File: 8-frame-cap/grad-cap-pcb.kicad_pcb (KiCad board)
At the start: 2 copper layers, 339.4 x 339.4 mm, 127 parts, among them J1 B02B-XASK-1LFSN, T1 PHPT610035PKX, T2 PHPT610035PKX, T3 PHPT610035PKX, T4 PHPT610035PKX, T5 PHPT610035PKX, T6 PHPT610035PKX, T7 PHPT610035PKX, U1 MC74HC73ADR2G, U2 SN74HCS238DYYR, U3 ICM7555xB, U4 SN74AHCT32DBR, U5 SN74AHCT32DBR

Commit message: routed traces, reorganized, renamed
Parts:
- removed the D50 at (334.5, 214.4)
- removed the D50 at (353.9, 236.1)
- added D18: 3, LED_SMD:LED_0805_2012Metric_Pad1.15x1.40mm_HandSolder, F.Cu at (213.0, 187.0)
- added D19: 1, LED_SMD:LED_0805_2012Metric_Pad1.15x1.40mm_HandSolder, F.Cu at (210.1, 229.4)
- added D50: 12, LED_SMD:LED_0805_2012Metric_Pad1.15x1.40mm_HandSolder, F.Cu at (321.2, 211.4)
- added D51: 2, LED_SMD:LED_0805_2012Metric_Pad1.15x1.40mm_HandSolder, F.Cu at (298.1, 207.4)
- added D52: 23, LED_SMD:LED_0805_2012Metric_Pad1.15x1.40mm_HandSolder, F.Cu at (285.7, 216.7)
- added D53: 3, LED_SMD:LED_0805_2012Metric_Pad1.15x1.40mm_HandSolder, F.Cu at (280.2, 228.5)
- added D54: 3, LED_SMD:LED_0805_2012Metric_Pad1.15x1.40mm_HandSolder, F.Cu at (325.6, 202.8)
- added D55: 1, LED_SMD:LED_0805_2012Metric_Pad1.15x1.40mm_HandSolder, F.Cu at (321.0, 188.1)
- added D56: 12, LED_SMD:LED_0805_2012Metric_Pad1.15x1.40mm_HandSolder, F.Cu at (312.9, 174.9)
- added D57: 2, LED_SMD:LED_0805_2012Metric_Pad1.15x1.40mm_HandSolder, F.Cu at (295.0, 166.0)
- added D58: 23, LED_SMD:LED_0805_2012Metric_Pad1.15x1.40mm_HandSolder, F.Cu at (340.6, 198.6)
- added D59: 3, LED_SMD:LED_0805_2012Metric_Pad1.15x1.40mm_HandSolder, F.Cu at (347.5, 186.7)
- added D60: 3, LED_SMD:LED_0805_2012Metric_Pad1.15x1.40mm_HandSolder, F.Cu at (358.3, 177.0)
- added D61: 1, LED_SMD:LED_0805_2012Metric_Pad1.15x1.40mm_HandSolder, F.Cu at (356.2, 215.0)
- added D62: 12, LED_SMD:LED_0805_2012Metric_Pad1.15x1.40mm_HandSolder, F.Cu at (375.9, 217.4)
- added D63: 2, LED_SMD:LED_0805_2012Metric_Pad1.15x1.40mm_HandSolder, F.Cu at (391.1, 224.6)
- added D64: 23, LED_SMD:LED_0805_2012Metric_Pad1.15x1.40mm_HandSolder, F.Cu at (341.6, 228.1)
- added D65: 3, LED_SMD:LED_0805_2012Metric_Pad1.15x1.40mm_HandSolder, F.Cu at (348.6, 242.1)
- added D66: 3, LED_SMD:LED_0805_2012Metric_Pad1.15x1.40mm_HandSolder, F.Cu at (350.0, 256.0)
- added D67: 1, LED_SMD:LED_0805_2012Metric_Pad1.15x1.40mm_HandSolder, F.Cu at (350.0, 270.0)
- added G***: LOGO, LOGO, F.Cu at (253.8, 102.2)
- added R31: R_Small_US, Resistor_SMD:R_0603_1608Metric_Pad0.98x0.95mm_HandSolder, F.Cu at (245.0, 153.0)
- added R63: R_Small_US, Resistor_SMD:R_0603_1608Metric_Pad0.98x0.95mm_HandSolder, F.Cu at (386.1, 222.4)
- added R64: R_Small_US, Resistor_SMD:R_0603_1608Metric_Pad0.98x0.95mm_HandSolder, F.Cu at (345.6, 234.1)
- added R65: R_Small_US, Resistor_SMD:R_0603_1608Metric_Pad0.98x0.95mm_HandSolder, F.Cu at (350.0, 248.0)
- added R66: R_Small_US, Resistor_SMD:R_0603_1608Metric_Pad0.98x0.95mm_HandSolder, F.Cu at (350.0, 261.0)
- added R67: R_Small_US, Resistor_SMD:R_0603_1608Metric_Pad0.98x0.95mm_HandSolder, F.Cu at (350.0, 276.0)
- added R68: R_Small_US, Resistor_SMD:R_0603_1608Metric_Pad0.98x0.95mm_HandSolder, F.Cu at (257.1, 375.2)
- added R69: R_Small_US, Resistor_SMD:R_0603_1608Metric_Pad0.98x0.95mm_HandSolder, F.Cu at (255.4, 377.0)
- added R70: 10K, Capacitor_SMD:C_0402_1005Metric_Pad0.74x0.62mm_HandSolder, F.Cu at (238.2, 370.0)
- added R71: 10K, Capacitor_SMD:C_0402_1005Metric_Pad0.74x0.62mm_HandSolder, F.Cu at (267.0, 362.3)
- added R72: 10k, Capacitor_SMD:C_0402_1005Metric_Pad0.74x0.62mm_HandSolder, B.Cu at (251.8, 354.6)
- added R73: 10k, Capacitor_SMD:C_0402_1005Metric_Pad0.74x0.62mm_HandSolder, B.Cu at (250.2, 354.6)
- added R74: 10k, Capacitor_SMD:C_0402_1005Metric_Pad0.74x0.62mm_HandSolder, B.Cu at (248.7, 354.6)
- added R75: 10k, Capacitor_SMD:C_0402_1005Metric_Pad0.74x0.62mm_HandSolder, F.Cu at (291.1, 364.0)
- added R76: 10k, Capacitor_SMD:C_0402_1005Metric_Pad0.74x0.62mm_HandSolder, F.Cu at (291.1, 366.0)
- added R77: 10k, Capacitor_SMD:C_0402_1005Metric_Pad0.74x0.62mm_HandSolder, F.Cu at (291.1, 368.0)
- added R78: 10k, Capacitor_SMD:C_0402_1005Metric_Pad0.74x0.62mm_HandSolder, F.Cu at (226.1, 351.0)
- added R79: 10k, Capacitor_SMD:C_0402_1005Metric_Pad0.74x0.62mm_HandSolder, F.Cu at (226.1, 353.0)
- added R80: 10k, Capacitor_SMD:C_0402_1005Metric_Pad0.74x0.62mm_HandSolder, F.Cu at (226.1, 355.0)
- added R81: 10K, Capacitor_SMD:C_0402_1005Metric_Pad0.74x0.62mm_HandSolder, F.Cu at (238.1, 365.0)
- added R82: 10K, Capacitor_SMD:C_0402_1005Metric_Pad0.74x0.62mm_HandSolder, F.Cu at (241.6, 358.3)
- added R83: 10K, Capacitor_SMD:C_0402_1005Metric_Pad0.74x0.62mm_HandSolder, F.Cu at (235.2, 370.0)
- added R84: 10K, Capacitor_SMD:C_0402_1005Metric_Pad0.74x0.62mm_HandSolder, F.Cu at (267.0, 364.8)
- added U6: MC74HC73ADR2G, GRAD-CAP:MC74HC73ADR2G_JK-FLIPFLOP, F.Cu at (259.0, 360.5)
- C1: value C_Small_US -> C_Small; footprint Capacitor_SMD:C_0805_2012Metric_Pad1.18x1.45mm_HandSolder -> Capacitor_SMD:C_0603_1608Metric_Pad1.08x0.95mm_HandSolder
- C2: value .1uF -> C_Small_US; footprint Capacitor_SMD:C_0805_2012Metric_Pad1.18x1.45mm_HandSolder -> Capacitor_SMD:C_0603_1608Metric_Pad1.08x0.95mm_HandSolder
- C3: value C_Small -> .1uF; footprint Capacitor_SMD:C_0805_2012Metric_Pad1.18x1.45mm_HandSolder -> Capacitor_SMD:C_0603_1608Metric_Pad1.08x0.95mm_HandSolder; moved to B.Cu
- D1, D28, D36, D8: footprint LED_SMD:LED_0603_1608Metric -> LED_SMD:LED_0805_2012Metric_Pad1.15x1.40mm_HandSolder
- D10: value 12 -> 23; footprint LED_SMD:LED_0603_1608Metric -> LED_SMD:LED_0805_2012Metric_Pad1.15x1.40mm_HandSolder
- D11, D30: value 6 -> 3; footprint LED_SMD:LED_0603_1608Metric -> LED_SMD:LED_0805_2012Metric_Pad1.15x1.40mm_HandSolder
- D12, D23, D24: value 67 -> 3; footprint LED_SMD:LED_0603_1608Metric -> LED_SMD:LED_0805_2012Metric_Pad1.15x1.40mm_HandSolder
- D13: value 56 -> 1; footprint LED_SMD:LED_0603_1608Metric -> LED_SMD:LED_0805_2012Metric_Pad1.15x1.40mm_HandSolder
- D14: value 6 -> 12; footprint LED_SMD:LED_0603_1608Metric -> LED_SMD:LED_0805_2012Metric_Pad1.15x1.40mm_HandSolder
- D15: value 6 -> 2; footprint LED_SMD:LED_0603_1608Metric -> LED_SMD:LED_0805_2012Metric_Pad1.15x1.40mm_HandSolder
- D16: value 1 -> 23; footprint LED_SMD:LED_0603_1608Metric -> LED_SMD:LED_0805_2012Metric_Pad1.15x1.40mm_HandSolder
- D17, D42: value 23 -> 3; footprint LED_SMD:LED_0603_1608Metric -> LED_SMD:LED_0805_2012Metric_Pad1.15x1.40mm_HandSolder
- D2, D32: value 4 -> 12; footprint LED_SMD:LED_0603_1608Metric -> LED_SMD:LED_0805_2012Metric_Pad1.15x1.40mm_HandSolder
- D20: value 2 -> 12; footprint LED_SMD:LED_0603_1608Metric -> LED_SMD:LED_0805_2012Metric_Pad1.15x1.40mm_HandSolder
- D21: value 67 -> 2; footprint LED_SMD:LED_0603_1608Metric -> LED_SMD:LED_0805_2012Metric_Pad1.15x1.40mm_HandSolder
- D22: value 7 -> 23; footprint LED_SMD:LED_0603_1608Metric -> LED_SMD:LED_0805_2012Metric_Pad1.15x1.40mm_HandSolder
- D25: value 6 -> 1; footprint LED_SMD:LED_0603_1608Metric -> LED_SMD:LED_0805_2012Metric_Pad1.15x1.40mm_HandSolder
- D26: value 32 -> 12; footprint LED_SMD:LED_0603_1608Metric -> LED_SMD:LED_0805_2012Metric_Pad1.15x1.40mm_HandSolder
- D27: value 1 -> 2; footprint LED_SMD:LED_0603_1608Metric -> LED_SMD:LED_0805_2012Metric_Pad1.15x1.40mm_HandSolder
- D29: value 7 -> 3; footprint LED_SMD:LED_0603_1608Metric -> LED_SMD:LED_0805_2012Metric_Pad1.15x1.40mm_HandSolder
- D3: value 56 -> 2; footprint LED_SMD:LED_0603_1608Metric -> LED_SMD:LED_0805_2012Metric_Pad1.15x1.40mm_HandSolder
- D31: value 7 -> 1; footprint LED_SMD:LED_0603_1608Metric -> LED_SMD:LED_0805_2012Metric_Pad1.15x1.40mm_HandSolder
- D33, D45: value 7 -> 2; footprint LED_SMD:LED_0603_1608Metric -> LED_SMD:LED_0805_2012Metric_Pad1.15x1.40mm_HandSolder
- D34: value 3 -> 23; footprint LED_SMD:LED_0603_1608Metric -> LED_SMD:LED_0805_2012Metric_Pad1.15x1.40mm_HandSolder
- D35: value 12 -> 3; footprint LED_SMD:LED_0603_1608Metric -> LED_SMD:LED_0805_2012Metric_Pad1.15x1.40mm_HandSolder
- D37: value 8 -> 1; footprint LED_SMD:LED_0603_1608Metric -> LED_SMD:LED_0805_2012Metric_Pad1.15x1.40mm_HandSolder
- D38: value 67 -> 12; footprint LED_SMD:LED_0603_1608Metric -> LED_SMD:LED_0805_2012Metric_Pad1.15x1.40mm_HandSolder
- D39: value 45 -> 2; footprint LED_SMD:LED_0603_1608Metric -> LED_SMD:LED_0805_2012Metric_Pad1.15x1.40mm_HandSolder
- D4, D46: value 5 -> 23; footprint LED_SMD:LED_0603_1608Metric -> LED_SMD:LED_0805_2012Metric_Pad1.15x1.40mm_HandSolder
- D40: value 8 -> 23; footprint LED_SMD:LED_0603_1608Metric -> LED_SMD:LED_0805_2012Metric_Pad1.15x1.40mm_HandSolder
- D41: value 8 -> 3; footprint LED_SMD:LED_0603_1608Metric -> LED_SMD:LED_0805_2012Metric_Pad1.15x1.40mm_HandSolder
- D43: value 3 -> 1; footprint LED_SMD:LED_0603_1608Metric -> LED_SMD:LED_0805_2012Metric_Pad1.15x1.40mm_HandSolder
- D44: value 5 -> 12; footprint LED_SMD:LED_0603_1608Metric -> LED_SMD:LED_0805_2012Metric_Pad1.15x1.40mm_HandSolder
- D47: value 5 -> 3; footprint LED_SMD:LED_0603_1608Metric -> LED_SMD:LED_0805_2012Metric_Pad1.15x1.40mm_HandSolder
- D48: value 81 -> 3; footprint LED_SMD:LED_0603_1608Metric -> LED_SMD:LED_0805_2012Metric_Pad1.15x1.40mm_HandSolder
- D49: value 81 -> 1; footprint LED_SMD:LED_0603_1608Metric -> LED_SMD:LED_0805_2012Metric_Pad1.15x1.40mm_HandSolder
- D5, D6: value 56 -> 3; footprint LED_SMD:LED_0603_1608Metric -> LED_SMD:LED_0805_2012Metric_Pad1.15x1.40mm_HandSolder
- D7: value 12 -> 1; footprint LED_SMD:LED_0603_1608Metric -> LED_SMD:LED_0805_2012Metric_Pad1.15x1.40mm_HandSolder
- D9: value 12 -> 2; footprint LED_SMD:LED_0603_1608Metric -> LED_SMD:LED_0805_2012Metric_Pad1.15x1.40mm_HandSolder
- R1, R3: value 10K -> R_Small_US; footprint Resistor_SMD:R_0805_2012Metric_Pad1.20x1.40mm_HandSolder -> Resistor_SMD:R_0603_1608Metric_Pad0.98x0.95mm_HandSolder
- R10, R11, R12, R13, R5, R6, R7, R8, R9: value 10k -> R_Small_US; footprint Capacitor_SMD:C_0805_2012Metric_Pad1.18x1.45mm_HandSolder -> Resistor_SMD:R_0603_1608Metric_Pad0.98x0.95mm_HandSolder
- R14, R15, R16, R17, R18, R19, R2, R20, R21, R22, R23, R24, R25, R26, R27, R28, R29, R30, R32, R33, R34, R35, R36, R37, R38, R39, R4, R40, R41, R42, R43, R44, R45, R46, R47, R48, R49, R50, R51, R52, R53, R54, R55, R56, R57, R58, R59, R60, R61, R62: footprint Resistor_SMD:R_0805_2012Metric_Pad1.20x1.40mm_HandSolder -> Resistor_SMD:R_0603_1608Metric_Pad0.98x0.95mm_HandSolder
- U1: value MC74HC73ADR2G -> ICM7555xB; footprint GRAD-CAP:MC74HC73ADR2G_JK-FLIPFLOP -> Package_SO:SOIC-8_3.9x4.9mm_P1.27mm
- U2: value SN74HCS238DYYR -> MC74HC73ADR2G; footprint GRAD-CAP:SN74HCS238DYYR-3-8-MUX -> GRAD-CAP:MC74HC73ADR2G_JK-FLIPFLOP
- U3: value ICM7555xB -> SN74HCS238DYYR; footprint Package_SO:SOIC-8_3.9x4.9mm_P1.27mm -> GRAD-CAP:SN74HCS238DYYR-3-8-MUX
- moved R30 188.5 mm to (175.7, 156.3), turned to 45 degrees
- moved D8 175.0 mm to (186.0, 263.0), turned to -112.5 degrees
- moved D9 171.5 mm to (185.0, 280.2), turned to -90 degrees
- moved D45 166.0 mm to (279.6, 293.8), turned to -112.5 degrees
- moved R12 163.1 mm to (139.0, 241.0), turned to -157.5 degrees
- moved D32 162.8 mm to (230.7, 131.7), turned to -45 degrees
- moved R49 156.2 mm to (333.0, 220.0), turned to 22.5 degrees
- moved R11 154.6 mm to (158.0, 234.0), turned to -157.5 degrees
- moved D17 151.7 mm to (208.0, 196.0), turned to -112.5 degrees
- moved R34 149.5 mm to (261.3, 140.7), turned to 45 degrees
- moved R50 146.3 mm to (316.0, 209.0), turned to -22.5 degrees
- moved R57 144.1 mm to (288.0, 165.0), turned to 0 degrees
- moved D33 142.6 mm to (213.0, 120.0), turned to -22.5 degrees
- moved D36 142.5 mm to (294.0, 117.0), turned to 180 degrees
- moved R13 139.8 mm to (185.0, 220.0), turned to 112.5 degrees
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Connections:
- C1 pad 1: /555-pin2-6 -> /555-pin5
- C2 pad 1: +3.3V -> /555-pin2-6
- C3 pad 1: /555-pin5 -> +3.3V
- R1 pad 1: +3.3V -> /leds+mosfets/6c
- R1 pad 2: /u4-pu-r2 -> Net-(D1-A)
- R10 pad 1: /leds+mosfets/u3-pd-3y -> /leds+mosfets/6or7
- R10 pad 2: GND -> Net-(D10-A)
- R11 pad 1: /leds+mosfets/u8-pd2y -> /leds+mosfets/6c
- R11 pad 2: GND -> Net-(D11-A)
- R12 pad 1: /leds+mosfets/u8-pd2b -> /leds+mosfets/1c
- R12 pad 2: GND -> Net-(D12-A)
- R13 pad 1: /leds+mosfets/u8-pd2a -> /leds+mosfets/6or7
- R13 pad 2: GND -> Net-(D13-A)
- R14 pad 1: /leds+mosfets/frame1 -> /leds+mosfets/6c
- R14 pad 2: Net-(D1-A) -> Net-(D14-A)
- R15 pad 1: /leds+mosfets/frame4 -> /leds+mosfets/1c
- R15 pad 2: Net-(D2-A) -> Net-(D15-A)
- R16 pad 1: /leds+mosfets/5or6 -> /leds+mosfets/6or7
- R16 pad 2: Net-(D3-A) -> Net-(D16-A)
- R17 pad 1: Net-(D4-A) -> /leds+mosfets/6c
- R17 pad 2: /leds+mosfets/frame5 -> Net-(D17-A)
- R18 pad 1: /leds+mosfets/5or6 -> /leds+mosfets/1c
- R18 pad 2: Net-(D5-A) -> Net-(D18-A)
- R19 pad 1: /leds+mosfets/5or6 -> /leds+mosfets/6or7
- R19 pad 2: Net-(D6-A) -> Net-(D19-A)
- R2 pad 1: 555-power -> /leds+mosfets/1c
- R2 pad 2: /555-pin7 -> Net-(D2-A)
- R20 pad 1: /leds+mosfets/1or2 -> /leds+mosfets/6c
- R20 pad 2: Net-(D7-A) -> Net-(D20-A)
- R21 pad 1: /leds+mosfets/1or2 -> /leds+mosfets/4c
- R21 pad 2: Net-(D8-A) -> Net-(D21-A)
- R22 pad 1: /leds+mosfets/1or2 -> /leds+mosfets/10c
- R22 pad 2: Net-(D9-A) -> Net-(D22-A)
- R23 pad 1: /leds+mosfets/1or2 -> /leds+mosfets/2or3
- R23 pad 2: Net-(D10-A) -> Net-(D23-A)
- R24 pad 1: /leds+mosfets/frame6 -> /leds+mosfets/6c
- R24 pad 2: Net-(D11-A) -> Net-(D24-A)
- R25 pad 1: /leds+mosfets/6or7 -> /leds+mosfets/2c
- R25 pad 2: Net-(D12-A) -> Net-(D25-A)
- R26 pad 1: Net-(D13-A) -> /leds+mosfets/2or3
- R26 pad 2: /leds+mosfets/5or6 -> Net-(D26-A)
- R27 pad 1: /leds+mosfets/frame6 -> /leds+mosfets/3c
- R27 pad 2: Net-(D14-A) -> Net-(D27-A)
- R28 pad 1: /leds+mosfets/frame6 -> /leds+mosfets/2or3
- R28 pad 2: Net-(D15-A) -> Net-(D28-A)
- R29 pad 1: /leds+mosfets/frame1 -> /leds+mosfets/3c
- R29 pad 2: Net-(D16-A) -> Net-(D29-A)
- R3 pad 1: +3.3V -> /leds+mosfets/1or2
- R3 pad 2: /ff-reset -> Net-(D3-A)
- R30 pad 1: /leds+mosfets/2or3 -> /leds+mosfets/4c
- R30 pad 2: Net-(D17-A) -> Net-(D30-A)
- R32 pad 1: /leds+mosfets/frame2 -> /leds+mosfets/2or3
- R32 pad 2: Net-(D20-A) -> Net-(D32-A)
- R33 pad 1: /leds+mosfets/6or7 -> /leds+mosfets/3c
- R33 pad 2: Net-(D21-A) -> Net-(D33-A)
- R34 pad 1: /leds+mosfets/frame7 -> /leds+mosfets/11c
- R34 pad 2: Net-(D22-A) -> Net-(D34-A)
- R35 pad 1: Net-(D23-A) -> /leds+mosfets/11c
- R35 pad 2: /leds+mosfets/6or7 -> Net-(D35-A)
- R36 pad 1: /leds+mosfets/6or7 -> /leds+mosfets/13c
- R36 pad 2: Net-(D24-A) -> Net-(D36-A)
- R37 pad 1: /leds+mosfets/frame6 -> /leds+mosfets/2c
- R37 pad 2: Net-(D25-A) -> Net-(D37-A)
- R38 pad 2: Net-(D26-A) -> Net-(D38-A)
- R39 pad 1: /leds+mosfets/frame1 -> /leds+mosfets/3c
- R39 pad 2: Net-(D27-A) -> Net-(D39-A)
- R4 pad 1: /555-pin7 -> /leds+mosfets/2or3
- R4 pad 2: /555-pin2-6 -> Net-(D4-A)
- R40 pad 1: /leds+mosfets/2or3 -> /leds+mosfets/4c
- R40 pad 2: Net-(D28-A) -> Net-(D40-A)
- R41 pad 1: /leds+mosfets/frame7 -> /leds+mosfets/1or2
- R41 pad 2: Net-(D29-A) -> Net-(D41-A)
- R42 pad 1: /leds+mosfets/frame6 -> /leds+mosfets/2or3
- R42 pad 2: Net-(D30-A) -> Net-(D42-A)
- R43 pad 1: Net-(D31-A) -> /leds+mosfets/3c
- R43 pad 2: /leds+mosfets/frame7 -> Net-(D43-A)
- R44 pad 1: /leds+mosfets/frame4 -> /leds+mosfets/6or7
- R44 pad 2: Net-(D32-A) -> Net-(D44-A)
- R45 pad 1: /leds+mosfets/frame7 -> /leds+mosfets/6c
- R45 pad 2: Net-(D33-A) -> Net-(D45-A)
- R46 pad 1: /leds+mosfets/frame3 -> /leds+mosfets/1c
- R46 pad 2: Net-(D34-A) -> Net-(D46-A)
- R47 pad 2: Net-(D35-A) -> Net-(D47-A)
- R48 pad 1: /leds+mosfets/frame3 -> /leds+mosfets/9c
- R48 pad 2: Net-(D36-A) -> Net-(D48-A)
- R49 pad 1: /leds+mosfets/frame8 -> /leds+mosfets/11c
- R49 pad 2: Net-(D37-A) -> Net-(D49-A)
- R5 pad 1: /pd-mux-g0 -> /leds+mosfets/3c
- R5 pad 2: GND -> Net-(D5-A)
- R50 pad 1: /leds+mosfets/6or7 -> /leds+mosfets/13c
- R50 pad 2: Net-(D38-A) -> Net-(D50-A)
- R51 pad 1: /leds+mosfets/4or5 -> /leds+mosfets/4c
- R51 pad 2: Net-(D39-A) -> Net-(D51-A)
- R52 pad 1: /leds+mosfets/frame8 -> /leds+mosfets/10c
- R52 pad 2: Net-(D40-A) -> Net-(D52-A)
- R53 pad 1: /leds+mosfets/frame8 -> /leds+mosfets/6or7
- R53 pad 2: Net-(D41-A) -> Net-(D53-A)
- R54 pad 1: /leds+mosfets/2or3 -> /leds+mosfets/13c
- R54 pad 2: Net-(D42-A) -> Net-(D54-A)
- R55 pad 1: /leds+mosfets/frame3 -> /leds+mosfets/4c
- R55 pad 2: Net-(D43-A) -> Net-(D55-A)
- R56 pad 1: /leds+mosfets/frame5 -> /leds+mosfets/10c
- R56 pad 2: Net-(D44-A) -> Net-(D56-A)
- R57 pad 1: /leds+mosfets/frame7 -> /leds+mosfets/6or7
- R57 pad 2: Net-(D45-A) -> Net-(D57-A)
- R58 pad 1: Net-(D46-A) -> /leds+mosfets/12c
- R58 pad 2: /leds+mosfets/frame5 -> Net-(D58-A)
- R59 pad 1: /leds+mosfets/frame5 -> /leds+mosfets/10c
- R59 pad 2: Net-(D47-A) -> Net-(D59-A)
- R6 pad 1: /pd-mux-g1 -> /leds+mosfets/4c
- R6 pad 2: GND -> Net-(D6-A)
- R60 pad 1: /leds+mosfets/8or1 -> /leds+mosfets/14c
- R60 pad 2: Net-(D48-A) -> Net-(D60-A)
- R61 pad 1: /leds+mosfets/8or1 -> /leds+mosfets/4c
- R61 pad 2: Net-(D49-A) -> Net-(D61-A)
- R62 pad 1: /leds+mosfets/8or1 -> /leds+mosfets/10c
- R7 pad 1: /pd-mux-g2 -> /leds+mosfets/6or7
- R7 pad 2: GND -> Net-(D7-A)
- R8 pad 1: /leds+mosfets/u3-pd-3b -> /leds+mosfets/6c
- R8 pad 2: GND -> Net-(D8-A)
- R9 pad 1: /leds+mosfets/u3-pd-3a -> /leds+mosfets/1c
- R9 pad 2: GND -> Net-(D9-A)
- T1 pad 2: f6or7 -> f1or8
- T1 pad 4: 2 -> 1
- T1 pad 5: /leds+mosfets/frame3 -> /leds+mosfets/2c
- T1 pad 6: /leds+mosfets/frame3 -> /leds+mosfets/2c
- T1 pad 7: /leds+mosfets/6or7 -> /leds+mosfets/1c
- T1 pad 8: /leds+mosfets/6or7 -> /leds+mosfets/1c
- T2 pad 2: 1 -> f3or4
- T2 pad 4: 6 -> f4or5
- T2 pad 5: /leds+mosfets/frame7 -> /leds+mosfets/4c
- T2 pad 6: /leds+mosfets/frame7 -> /leds+mosfets/4c
- T2 pad 7: /leds+mosfets/frame2 -> /leds+mosfets/3c
- T2 pad 8: /leds+mosfets/frame2 -> /leds+mosfets/3c
- T3 pad 2: 5 -> f2or3
- T3 pad 4: unconnected-(T3-BASE-Pad4) -> f7or8
- T3 pad 5: /leds+mosfets/frame5 -> /leds+mosfets/6c
- T3 pad 6: /leds+mosfets/frame5 -> /leds+mosfets/6c
- T3 pad 7: /leds+mosfets/frame6 -> /leds+mosfets/2or3
- T3 pad 8: /leds+mosfets/frame6 -> /leds+mosfets/2or3
- T4 pad 2: 3 -> f1or2
- T4 pad 4: f4or5 -> f6or7
- T4 pad 5: /leds+mosfets/4or5 -> /leds+mosfets/6or7
- T4 pad 6: /leds+mosfets/4or5 -> /leds+mosfets/6or7
- T4 pad 7: /leds+mosfets/frame4 -> /leds+mosfets/1or2
- T4 pad 8: /leds+mosfets/frame4 -> /leds+mosfets/1or2
- T5 pad 2: f5or6 -> 2
- T5 pad 4: 0 -> f5or6
- T5 pad 5: /leds+mosfets/frame1 -> /leds+mosfets/10c
- T5 pad 6: /leds+mosfets/frame1 -> /leds+mosfets/10c
- T5 pad 7: /leds+mosfets/5or6 -> /leds+mosfets/9c
- T5 pad 8: /leds+mosfets/5or6 -> /leds+mosfets/9c
- T6 pad 2: 7 -> 3
- T6 pad 4: f1or8 -> 5
- T6 pad 5: /leds+mosfets/8or1 -> /leds+mosfets/12c
- T6 pad 6: /leds+mosfets/8or1 -> /leds+mosfets/12c
- T6 pad 7: /leds+mosfets/frame8 -> /leds+mosfets/11c
- T6 pad 8: /leds+mosfets/frame8 -> /leds+mosfets/11c
- T7 pad 2: f1or2 -> 4
- T7 pad 4: f2or3 -> 6
- T7 pad 5: /leds+mosfets/2or3 -> /leds+mosfets/14c
- T7 pad 6: /leds+mosfets/2or3 -> /leds+mosfets/14c
- T7 pad 7: /leds+mosfets/1or2 -> /leds+mosfets/13c
- T7 pad 8: /leds+mosfets/1or2 -> /leds+mosfets/13c
- U1 pad 1: CLOCK1 -> GND
- U1 pad 2: /ff-reset -> /555-pin2-6
- U1 pad 3: /ff-reset -> 555-PULSE
- U1 pad 4: +3.3V -> Net-(U1-R)
- U1 pad 5: CLOCK2 -> /555-pin5
- U1 pad 6: /ff-reset -> /555-pin2-6
- U1 pad 7: /ff-reset -> /555-pin7
- U1 pad 8: unconnected-(U1-*Q2-Pad8) -> Net-(U1-R)
- U2 pad 1: CLOCK1 -> 555-PULSE
- U2 pad 10: 5 -> /u4-pu-r2
- U2 pad 11: 4 -> GND
- U2 pad 12: 3 -> CLOCK1
- U2 pad 13: 2 -> Net-(U2-*Q1)
- U2 pad 14: 1 -> /u4-pu-r2
- U2 pad 2: CLOCK2 -> /ff-reset
- U2 pad 3: CLOCK3 -> /ff-reset
- U2 pad 4: /pd-mux-g0 -> +3.3V
- U2 pad 5: /pd-mux-g1 -> CLOCK1
- U2 pad 6: /pd-mux-g2 -> /ff-reset
- U2 pad 7: 7 -> /ff-reset
- U2 pad 8: GND -> Net-(U2-*Q1)
- U2 pad 9: 6 -> CLOCK2
- U3 pad 1: GND -> CLOCK1
- U3 pad 2: /555-pin2-6 -> CLOCK2
- U3 pad 3: CLOCK1 -> CLOCK3
- U3 pad 4: 555-power -> /pd-mux-g0
- U3 pad 5: /555-pin5 -> /pd-mux-g1
- U3 pad 6: /555-pin2-6 -> /pd-mux-g2
- U3 pad 7: /555-pin7 -> 7
- U3 pad 8: 555-power -> GND
- U5 pad 10: /leds+mosfets/u8-pd2a -> 7
- U5 pad 8: /leds+mosfets/u8-pd2y -> f7or8
- U5 pad 9: /leds+mosfets/u8-pd2b -> 6
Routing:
- net /leds+mosfets/6or7: track 0.00 -> 593.1 mm, vias 0 -> 8
- net /leds+mosfets/4c: track 0.00 -> 498.6 mm, vias 0 -> 11
- net /leds+mosfets/3c: track 0.00 -> 458.8 mm, vias 0 -> 6
- net /leds+mosfets/10c: track 0.00 -> 458.6 mm, vias 0 -> 6
- net /leds+mosfets/2or3: track 0.00 -> 407.3 mm, vias 0 -> 2
- net /leds+mosfets/1c: track 0.00 -> 369.1 mm, vias 0 -> 6
- net /leds+mosfets/6c: track 0.00 -> 360.8 mm, vias 0 -> 4
- net /leds+mosfets/13c: track 0.00 -> 299.2 mm, vias 0 -> 6
- net /leds+mosfets/11c: track 0.00 -> 290.5 mm, vias 0 -> 6
- net /leds+mosfets/1or2: track 0.00 -> 257.5 mm, vias 1 -> 10
- net /leds+mosfets/2c: track 0.00 -> 215.6 mm, vias 0 -> 4
- net /leds+mosfets/14c: track 0.00 -> 197.4 mm, vias 0 -> 4
- net /leds+mosfets/12c: track 0.00 -> 167.8 mm, vias 0 -> 4
- net /leds+mosfets/9c: track 0.00 -> 140.0 mm, vias 0 -> 2
- net CLOCK1: track 37.4 -> 9.35 mm, vias 2 -> 0
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- removed copper zone on F.Cu, net +3.3V
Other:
- board text removed: "1"
- board text removed: "2"
- board text removed: "24 cm"
- board text removed: "3"
- board text removed: "4"
- board text removed: "5"
- board text removed: "6"
- board text removed: "7"
- board text removed: "8"
- board text removed: "chud - billions must graduate chicken on raft"
- board text removed: "little bigger than 2 cm"
- board text removed: "w"

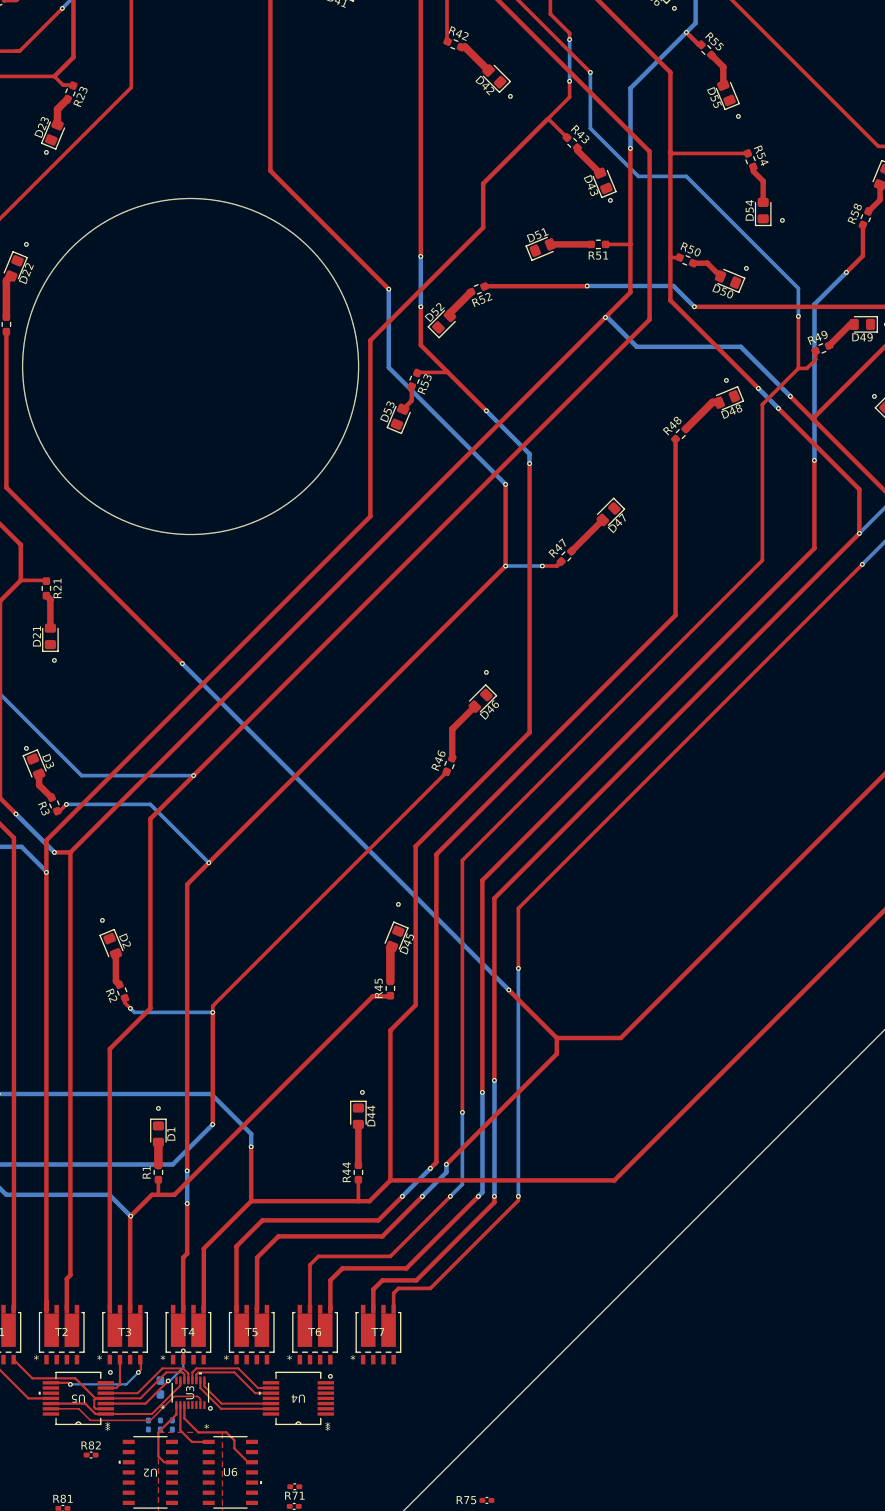
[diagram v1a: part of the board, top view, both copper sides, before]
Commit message: reorganized
horizontal -> vertical pin headers
traces added
moved components
switched clocks crystal-> si
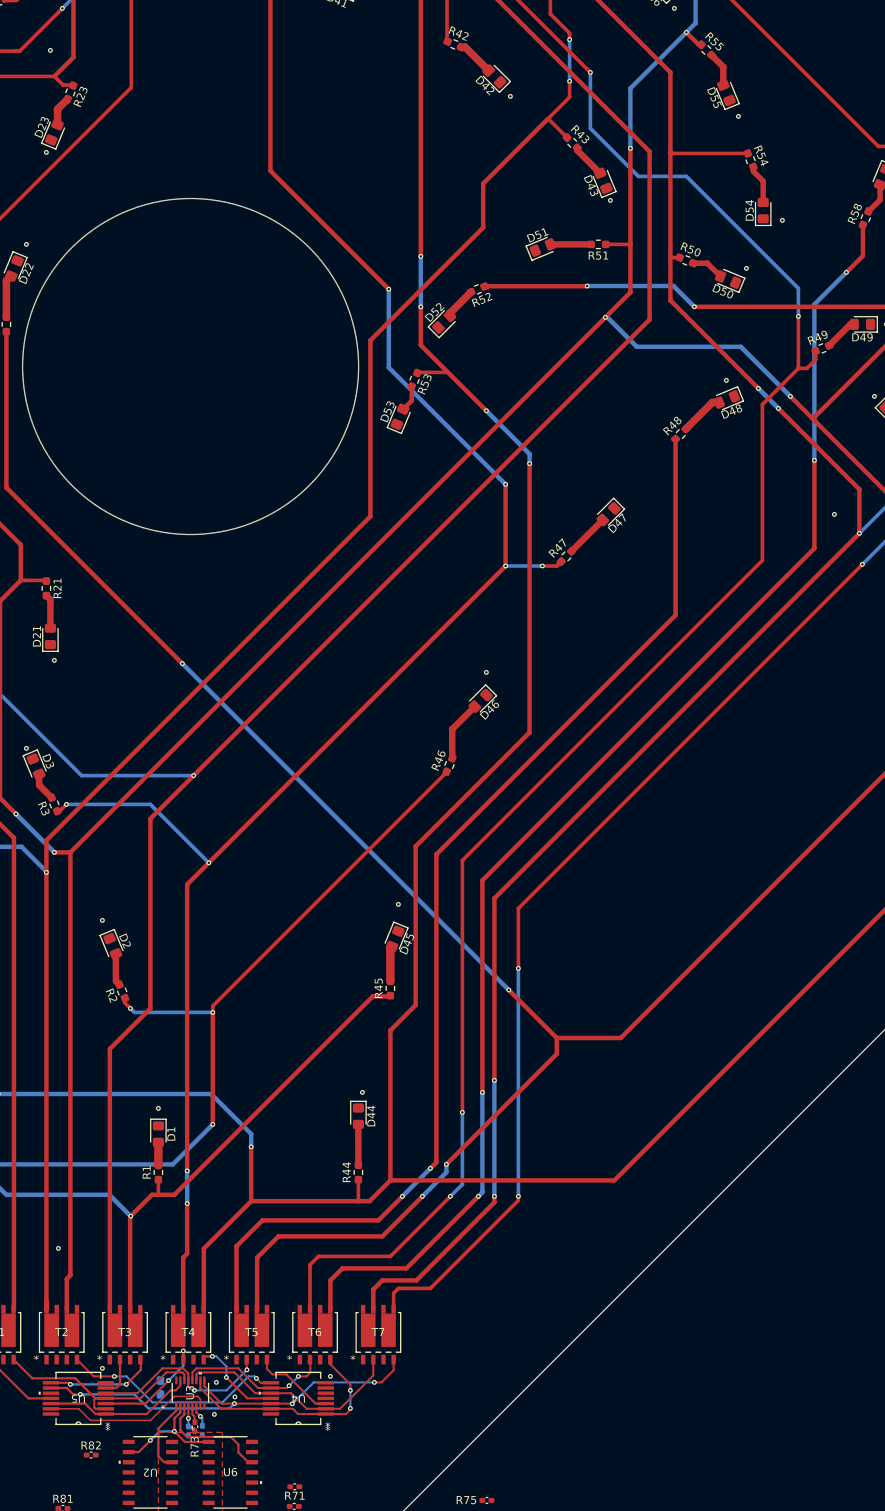
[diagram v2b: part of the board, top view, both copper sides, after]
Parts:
- R73: moved to F.Cu
- moved R74 6.78 mm to (255.5, 355.2)
- moved R73 4.32 mm to (254.6, 354.8)
- moved R72 2.14 mm to (253.8, 355.3)
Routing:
- net 6: track 9.96 -> 52.6 mm, vias 0 -> 4
- net f4or5: track 0.00 -> 28.1 mm, vias 0 -> 2
- net 5: track 10.9 -> 28.6 mm, vias 0 -> 2
- net 4: track 11.2 -> 28.6 mm
- net f6or7: track 0.00 -> 11.7 mm, vias 0 -> 2
- net 2: track 12.7 -> 23.4 mm, vias 0 -> 2
- net f5or6: track 0.00 -> 10.3 mm
- net CLOCK2: track 7.31 -> 15.2 mm, vias 0 -> 2
- net 3: track 12.0 -> 19.4 mm, vias 0 -> 2
- net /pd-mux-g2: track 0.00 -> 2.91 mm, vias 0 -> 1
- net /pd-mux-g0: track 0.00 -> 2.66 mm, vias 0 -> 1
- net /pd-mux-g1: track 0.00 -> 2.02 mm
- net CLOCK3: track 13.0 -> 14.6 mm
- net GND: vias 67 -> 71
- net (no net): vias 0 -> 1

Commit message: updated pcb
error checking
90* angles removal
schematic relinking
reorganizing schematic
fixed footprints for PHPT6 (mosfets, they didnt like the pads and the body being "different" pours or something)
silkscreen reorg
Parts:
- removed R78, R79, R80: 10k, Capacitor_SMD:C_0402_1005Metric_Pad0.74x0.62mm_HandSolder
- added C4: .1uF, Capacitor_SMD:C_0603_1608Metric_Pad1.08x0.95mm_HandSolder, B.Cu at (249.8, 358.6)
- added G***: LOGO, LOGO, B.Cu at (280.0, 180.0)
- C1: value C_Small -> .68uF
- C2: value C_Small_US -> .1uF; moved to B.Cu
- D1, D13, D19, D25, D31, D37, D43, D49, D55, D61, D67, D7: value 1 -> ~
- D10, D16, D22, D28, D34, D4, D40, D46, D52, D58, D64: value 23 -> ~
- D11, D12, D17, D18, D23, D24, D29, D30, D35, D36, D41, D42, D47, D48, D5, D53, D54, D59, D6, D60, D65, D66: value 3 -> ~
- D14, D2, D20, D26, D32, D38, D44, D50, D56, D62, D8: value 12 -> ~
- D15, D21, D27, D3, D33, D39, D45, D51, D57, D63, D9: value 2 -> ~
- R68: value R_Small_US -> 1M
- R69: value R_Small_US -> 270k
- R70, R71, R72, R74, R81, R82: footprint Capacitor_SMD:C_0402_1005Metric_Pad0.74x0.62mm_HandSolder -> Resistor_SMD:R_0603_1608Metric_Pad0.98x0.95mm_HandSolder
- R73, R75, R76, R77, R83, R84: footprint Capacitor_SMD:C_0402_1005Metric_Pad0.74x0.62mm_HandSolder -> Resistor_SMD:R_0603_1608Metric_Pad0.98x0.95mm_HandSolder; moved to B.Cu
- U1: value ICM7555xB -> MIC1557YM5-TR; footprint Package_SO:SOIC-8_3.9x4.9mm_P1.27mm -> GRAD-CAP:MIC1557
- moved R83 33.0 mm to (266.7, 360.2)
- moved R81 28.8 mm to (266.8, 363.3), turned to 180 degrees
- moved R84 25.2 mm to (242.3, 359.7), turned to 0 degrees
- moved R71 25.0 mm to (242.0, 362.8), turned to 0 degrees
- moved R77 23.6 mm to (276.4, 349.5), turned to 0 degrees
- moved R76 20.6 mm to (276.4, 351.5), turned to 0 degrees
- moved C2 18.2 mm to (259.1, 359.5), turned to 0 degrees
- moved R75 18.1 mm to (276.4, 353.4), turned to 0 degrees
- moved R82 17.4 mm to (256.9, 366.6), turned to 180 degrees
- moved R70 15.8 mm to (253.5, 365.8), turned to 90 degrees
- moved R69 8.01 mm to (251.0, 370.3), turned to 90 degrees
- moved C1 2.57 mm to (251.9, 373.7)
- moved R74 1.96 mm to (257.4, 355.6)
- moved R68 1.68 mm to (256.6, 373.6)
- moved R73 1.27 mm to (255.5, 355.6)
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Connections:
- net /leds+mosfets/u3-pd-3a renamed /u3-pd-3a
- net /leds+mosfets/u3-pd-3b renamed /u3-pd-3b
- net /leds+mosfets/u3-pd-3y renamed /u3-pd-3y
- net f3or4 renamed /3b
- C1 pad 1: /555-pin5 -> Net-(U1-T/T)
- C2 pad 1: /555-pin2-6 -> +3.3V
- R68 pad 1: Net-(U1-R) -> +3.3V
- R68 pad 2: /555-pin7 -> Net-(U1-CS)
- R69 pad 1: /555-pin7 -> Net-(U1-T/T)
- R69 pad 2: /555-pin2-6 -> 557-PULSE
- R70 pad 2: /ff-reset -> /ff-reset1
- R71 pad 2: /u4-pu-r2 -> /u4-pu-r2-1
- R81 pad 2: /u4-pu-r2 -> /u4-pu-r2-2
- R82 pad 2: /ff-reset -> /ff-reset2
- T1 pad 2: f1or8 -> /1b
- T1 pad 4: 1 -> /2b
- T1 pad 6: /leds+mosfets/2c -> /2c
- T1 pad 8: /leds+mosfets/1c -> /1c
- T2 pad 4: f4or5 -> /4b
- T2 pad 6: /leds+mosfets/4c -> /4c
- T2 pad 8: /leds+mosfets/3c -> /3c
- T3 pad 2: f2or3 -> /5b
- T3 pad 4: f7or8 -> /6b
- T3 pad 6: /leds+mosfets/6c -> /6c
- T3 pad 8: /leds+mosfets/2or3 -> /5c
- T4 pad 2: f1or2 -> /7b
- T4 pad 4: f6or7 -> /8b
- T4 pad 6: /leds+mosfets/6or7 -> /8c
- T4 pad 8: /leds+mosfets/1or2 -> /7c
- T5 pad 2: 2 -> /9b
- T5 pad 4: f5or6 -> /10b
- T5 pad 6: /leds+mosfets/10c -> /10c
- T5 pad 8: /leds+mosfets/9c -> /9c
- T6 pad 2: 3 -> /11b
- T6 pad 4: 5 -> /12b
- T6 pad 6: /leds+mosfets/12c -> /12c
- T6 pad 8: /leds+mosfets/11c -> /11c
- T7 pad 2: 4 -> /13b
- T7 pad 4: 6 -> /14b
- T7 pad 6: /leds+mosfets/14c -> /14c
- T7 pad 8: /leds+mosfets/13c -> /13c
- U1 pad 1: GND -> Net-(U1-T/T)
- U1 pad 2: /555-pin2-6 -> GND
- U1 pad 3: 555-PULSE -> Net-(U1-CS)
- U1 pad 4: Net-(U1-R) -> +3.3V
- U1 pad 5: /555-pin5 -> 557-PULSE
- U2 pad 1: 555-PULSE -> 557-PULSE
- U2 pad 10: /u4-pu-r2 -> /u4-pu-r2-1
- U2 pad 14: /u4-pu-r2 -> /u4-pu-r2-1
- U2 pad 2: /ff-reset -> /ff-reset1
- U2 pad 3: /ff-reset -> /ff-reset1
- U2 pad 6: /ff-reset -> /ff-reset1
- U2 pad 7: /ff-reset -> /ff-reset1
- U6 pad 10: /u4-pu-r2 -> /u4-pu-r2-2
- U6 pad 14: /u4-pu-r2 -> /u4-pu-r2-2
- U6 pad 2: /ff-reset -> /ff-reset2
- U6 pad 3: /ff-reset -> /ff-reset2
- U6 pad 6: /ff-reset -> /ff-reset2
- U6 pad 7: /ff-reset -> /ff-reset2
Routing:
- net +3.3V: track 0.00 -> 179.8 mm, vias 0 -> 21
- net Net-(U6-*Q1): track 0.00 -> 20.7 mm, vias 0 -> 3
- net GND: track 0.00 -> 15.0 mm, vias 71 -> 83
- net /ff-reset1: track 0.00 -> 12.6 mm
- net /u4-pu-r2-2: track 0.00 -> 11.6 mm
- net /ff-reset2: track 0.00 -> 10.7 mm
- net /u4-pu-r2-1: track 0.00 -> 10.5 mm
- net Net-(U2-*Q1): track 0.00 -> 10.1 mm, vias 0 -> 2
- net 557-PULSE: track 0.00 -> 8.56 mm, vias 0 -> 2
- net CLOCK1: track 9.35 -> 15.8 mm
- net /u3-pd-3b: track 0.00 -> 5.99 mm, vias 0 -> 1
- net /u3-pd-3a: track 0.00 -> 5.22 mm, vias 0 -> 1
- net Net-(U1-T/T): track 0.00 -> 5.00 mm
- net /u3-pd-3y: track 0.00 -> 4.83 mm, vias 0 -> 1
- net 7: track 21.4 -> 25.2 mm, vias 0 -> 2
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- added copper zone on B.Cu, net +3.3V
- removed copper zone on F.Cu, net /ff-reset
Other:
- outline, holes or cut-outs redrawn
- rule pad_to_mask_clearance: 0 -> 0.05

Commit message: updated pcb
shrunk edge cuts
moved led matrix header (again)
added 3d file links
added mounting holes
added 3 on board buttons
fixed unused pin header connections
discovered polygon filled area default chamfer (i will be using this always now)
updated bom with new caps
added status LED for usbc power in
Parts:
- removed the G*** at (253.8, 102.2)
- added G***: LOGO, LOGO, F.Cu at (488.0, 135.7)
- added G***: LOGO, LOGO, F.Cu at (437.3, 132.7)
- added G***: LOGO, LOGO, F.Cu at (401.2, 131.8)
- added G***: LOGO, LOGO, F.Cu at (4.03, 428.0)
- added G***: LOGO, LOGO, F.Cu at (431.3, 108.4)
- added G***: LOGO, LOGO, F.Cu at (377.9, 479.1)
- added G***: LOGO, LOGO, F.Cu at (437.4, 312.7)
- added G***: LOGO, LOGO, F.Cu at (260.0, 486.1)
- added G***: LOGO, LOGO, F.Cu at (254.0, 104.2)
- moved G*** 73.6 mm to (315.6, 244.4)
- moved G*** 36.8 mm to (304.6, 271.0)
- moved D53 7.19 mm to (273.2, 226.8), turned to 45 degrees
- moved D22 6.49 mm to (235.0, 215.8), turned to -90 degrees
- moved R53 5.65 mm to (276.4, 223.4), turned to -135 degrees
- moved R22 5.15 mm to (235.0, 220.2)
- moved D1 4.50 mm to (250.0, 313.7)
- moved R1 4.50 mm to (250.0, 318.5)
- moved D52 2.54 mm to (283.2, 217.2)
- moved D23 2.01 mm to (237.9, 194.8)
- moved R52 1.58 mm to (288.3, 212.7)
- moved R23 1.35 mm to (240.2, 188.5)
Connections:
- net /3b renamed f3or4
- net /5c renamed /2or3
- net /7c renamed /1or2
- net /8c renamed /6or7
- T1 pad 2: /1b -> f1or8
- T1 pad 4: /2b -> 1
- T2 pad 4: /4b -> f4or5
- T3 pad 2: /5b -> f2or3
- T3 pad 4: /6b -> f7or8
- T4 pad 2: /7b -> f1or2
- T4 pad 4: /8b -> f6or7
- T5 pad 2: /9b -> 2
- T5 pad 4: /10b -> f5or6
- T6 pad 2: /11b -> 3
- T6 pad 4: /12b -> 5
- T7 pad 2: /13b -> 4
- T7 pad 4: /14b -> 6
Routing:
- net /leds+mosfets/6c: track 360.8 -> 365.3 mm
- net /leds+mosfets/6or7: track 593.0 -> 597.3 mm
- net /leds+mosfets/10c: track 458.5 -> 455.4 mm
- net Net-(D22-A): track 5.39 -> 2.56 mm
- net /leds+mosfets/2or3: track 407.3 -> 408.7 mm
- net Net-(D23-A): track 3.73 -> 5.18 mm
- net Net-(D52-A): track 4.07 -> 4.99 mm
- net Net-(D53-A): track 3.28 -> 2.76 mm
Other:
- board size 339.4 x 339.4 mm -> 378.4 x 339.4 mm

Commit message: updated silkscreen
added custom designs
- put them to the side
lowkey cant decide what to do with them, or if i put them at all
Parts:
- moved G*** 601.1 mm to (451.9, 27.2)
- moved G*** 368.0 mm to (471.0, 123.1)
- moved G*** 365.9 mm to (420.4, 157.3)
- moved G*** 158.2 mm to (473.6, 158.6)
- moved G*** 25.2 mm to (397.7, 106.8)
- moved G*** 22.5 mm to (485.4, 113.3)
- moved G*** 17.0 mm to (295.7, 256.6)
- moved G*** 14.1 mm to (433.1, 119.2)
- moved G*** 5.49 mm to (434.8, 104.3)
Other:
- outline, holes or cut-outs redrawn
